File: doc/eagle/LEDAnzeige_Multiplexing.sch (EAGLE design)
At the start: 13 parts, among them IC4 MAX7219CNG

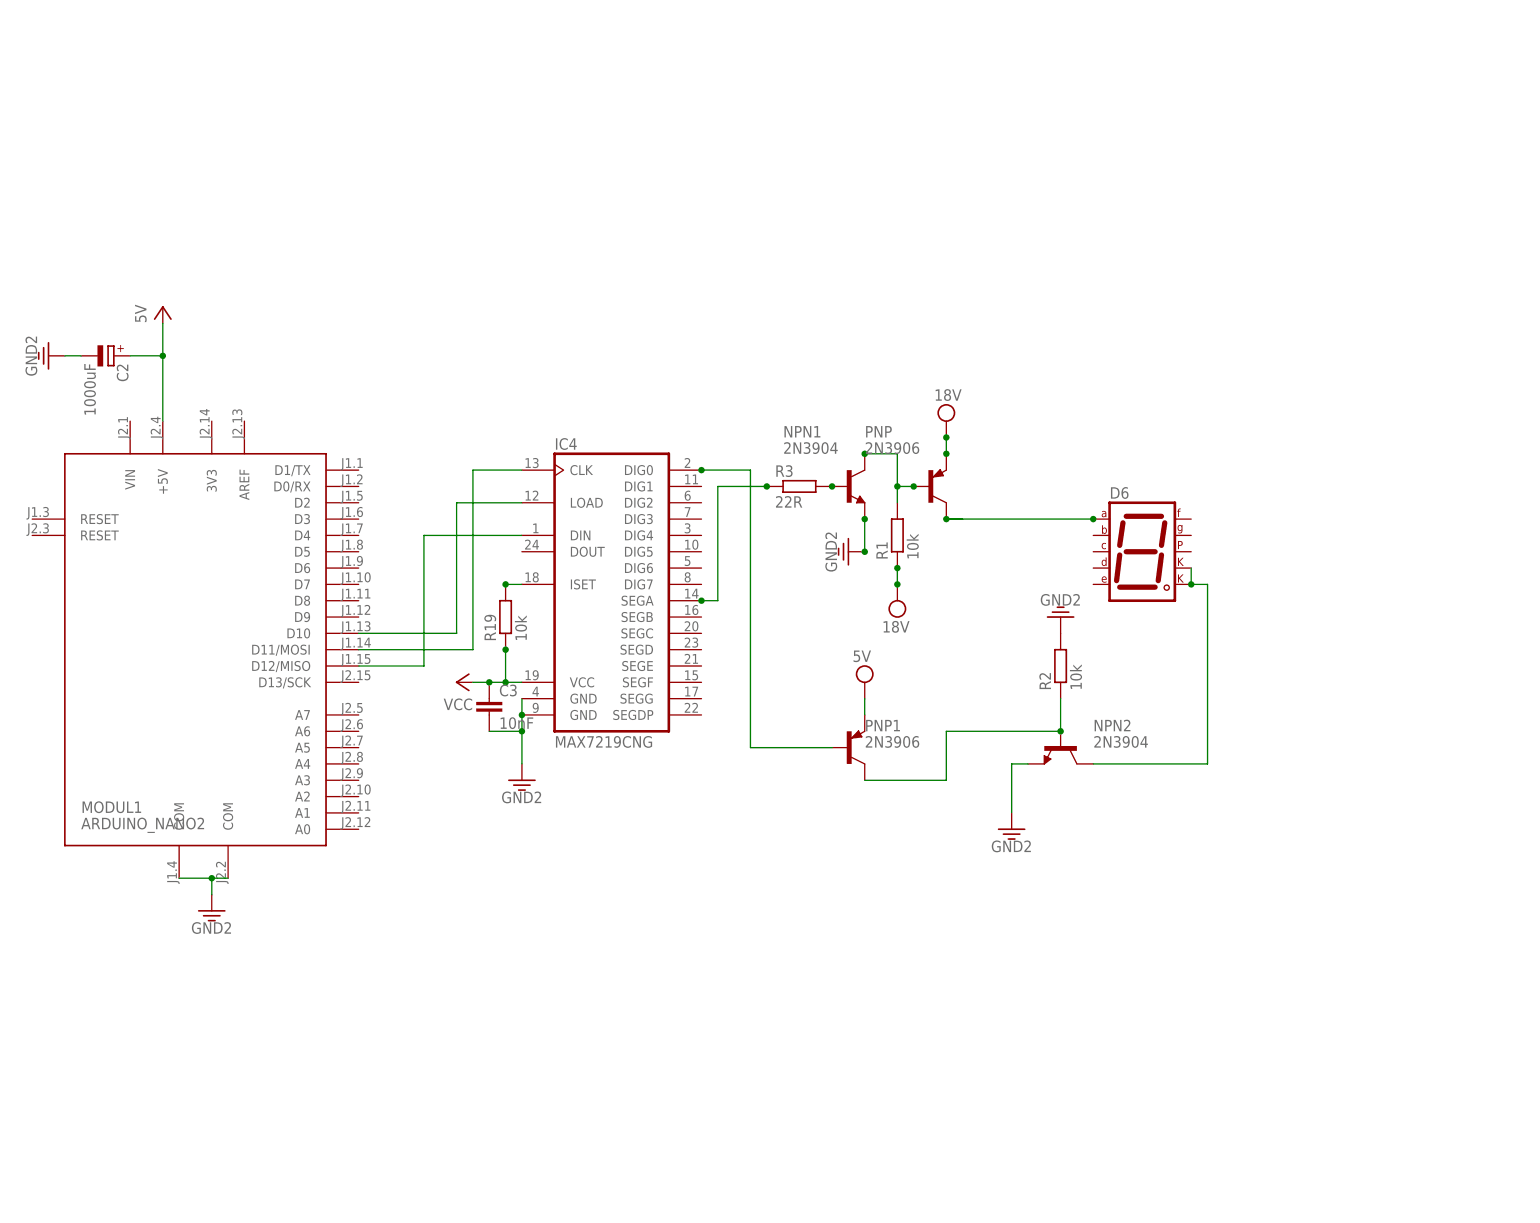
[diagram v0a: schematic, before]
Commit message: Schematic updated + Refactoring
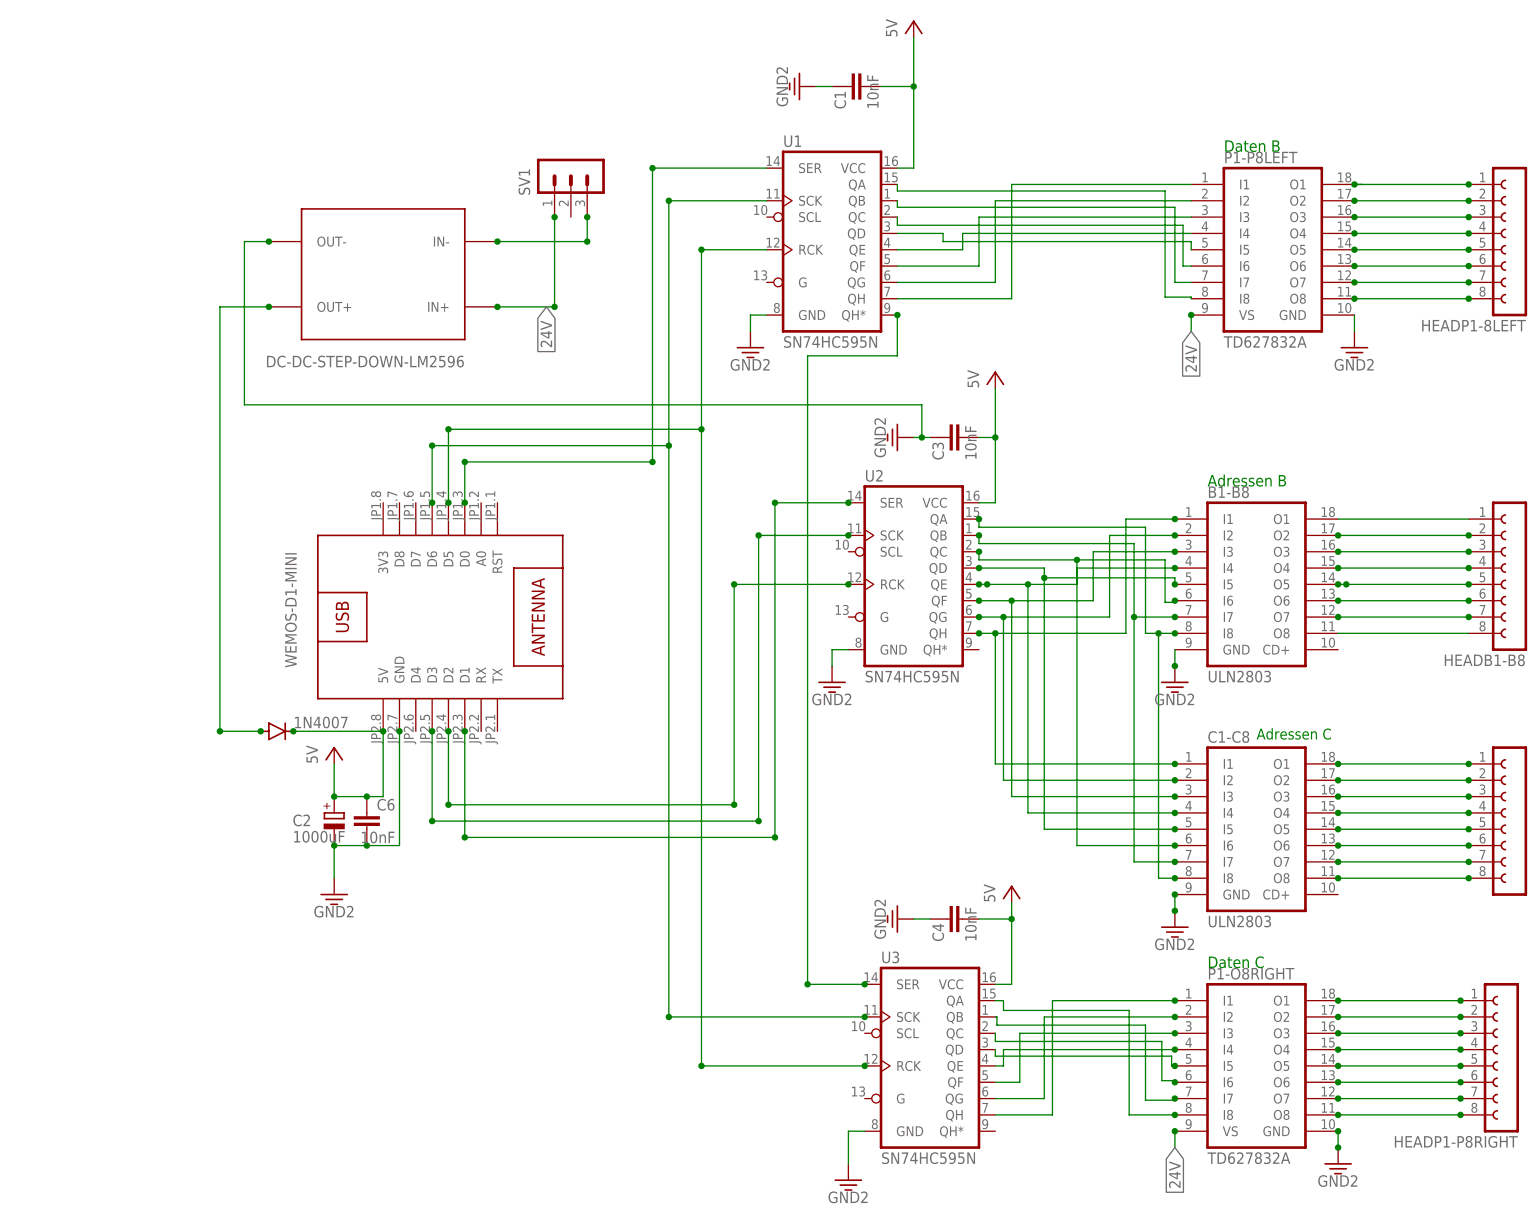
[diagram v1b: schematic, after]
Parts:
- removed D6: (no value), special:7SEG-MCK
- removed IC4: MAX7219CNG, maxim:MAX7219CNG
- removed MODUL1: ARDUINO_NANO2, arduino:ARDUINO_NANO2
- removed NPN1, NPN2: 2N3904, transistor-npn:2N3904
- removed PNP, PNP1: 2N3906, transistor-pnp:2N3906
- removed R1, R19, R2: 10k, resistor:R-EU_0204/7
- removed R3: 22R, resistor:R-EU_0204/7
- added 1N4007: (no value), diode:DIODE-D-2.5
- added B1-B8, C1-C8: ULN2803, uln-udn:ULN2803A
- added C1, C4, C6: 10nF, resistor:C-EU025-025X050
- added HEADB1-B8, HEADC1-C8, HEADP1-8LEFT, HEADP1-P8RIGHT: (no value), con-lsta:FE08-1
- added P1-O8RIGHT, P1-P8LEFT: TD627832A, td62083-dil:TD627832A
- added SV1: (no value), con-lstb:MA03-1
- added U$1: WEMOS-D1-MINI, diy-modules:WEMOS-D1-MINI
- added U$2: DC-DC-STEP-DOWN-LM2596, diy-modules_lm2596:DC-DC-STEP-DOWN-LM2596
- added U1, U2, U3: SN74HC595N, SparkFun-IC-Logic:74HC595N
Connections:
- removed net 3.3V: C2.-, C3.2, IC4.GND@1, IC4.GND@2, MODUL1.COM, MODUL1.COM@1, NPN1.E, NPN2.E, R2.2
- removed net N$101: IC4.CLK, MODUL1.D11/MOSI
- removed net N$102: IC4.LOAD, MODUL1.D10
- removed net N$103: IC4.DIN, MODUL1.D12/MISO
- new net 24V: P1-O8RIGHT.VS, P1-P8LEFT.VS, SV1.1, U$2.IN+
- new net GND: B1-B8.GND, C1-C8.GND, C1.1, C2.-, C3.1, C4.1, C6.2, P1-O8RIGHT.GND, P1-P8LEFT.GND, U$1.GND, U$2.OUT-, U1.GND, U2.GND, U3.GND
- new net N$10: HEADP1-8LEFT.3, P1-P8LEFT.O3
- new net N$11: HEADP1-8LEFT.4, P1-P8LEFT.O4
- new net N$12: HEADP1-8LEFT.5, P1-P8LEFT.O5
- new net N$13: HEADP1-8LEFT.6, P1-P8LEFT.O6
- new net N$14: HEADP1-8LEFT.7, P1-P8LEFT.O7
- new net N$15: HEADP1-8LEFT.8, P1-P8LEFT.O8
- new net N$16: B1-B8.O1, HEADB1-B8.1
- new net N$17: B1-B8.O2, HEADB1-B8.2
- new net N$18: B1-B8.O3, HEADB1-B8.3
- new net N$19: B1-B8.O4, HEADB1-B8.4
- new net N$20: HEADP1-8LEFT.1, P1-P8LEFT.O1
- new net N$21: B1-B8.O5, HEADB1-B8.5
- new net N$23: B1-B8.O7, HEADB1-B8.7
- new net N$24: B1-B8.O8, HEADB1-B8.8
- new net N$25: P1-P8LEFT.I1, U1.QH
- new net N$26: HEADP1-P8RIGHT.1, P1-O8RIGHT.O1
- new net N$27: P1-P8LEFT.I2, U1.QG
- new net N$28: HEADP1-P8RIGHT.3, P1-O8RIGHT.O3
- new net N$29: P1-P8LEFT.I3, U1.QF
- new net N$30: HEADP1-P8RIGHT.2, P1-O8RIGHT.O2
- new net N$31: P1-P8LEFT.I4, U1.QE
- new net N$32: P1-P8LEFT.I5, U1.QD
- new net N$33: HEADP1-P8RIGHT.5, P1-O8RIGHT.O5
- new net N$34: U$1.D0, U1.SER
- new net N$35: HEADP1-P8RIGHT.6, P1-O8RIGHT.O6
- new net N$37: U$1.D1, U2.SER
- new net N$39: HEADP1-P8RIGHT.4, P1-O8RIGHT.O4
- new net N$40: HEADP1-P8RIGHT.7, P1-O8RIGHT.O7
- new net N$42: P1-P8LEFT.I7, U1.QB
- new net N$43: P1-P8LEFT.I8, U1.QA
- new net N$44: P1-O8RIGHT.I2, U3.QG
- new net N$45: P1-O8RIGHT.I3, U3.QF
- new net N$46: P1-O8RIGHT.I4, U3.QE
- new net N$47: P1-O8RIGHT.I5, U3.QD
- new net N$48: P1-O8RIGHT.I6, U3.QC
- new net N$49: HEADP1-P8RIGHT.8, P1-O8RIGHT.O8
- new net N$5: B1-B8.I5, C1-C8.I5, U2.QD
- new net N$51: C1-C8.O2, HEADC1-C8.2
- new net N$52: C1-C8.O3, HEADC1-C8.3
- new net N$53: C1-C8.O4, HEADC1-C8.4
- new net N$54: C1-C8.O5, HEADC1-C8.5
- new net N$55: P1-O8RIGHT.I7, U3.QB
- new net N$56: P1-O8RIGHT.I8, U3.QA
- new net N$57: C1-C8.O6, HEADC1-C8.6
- new net N$58: C1-C8.O7, HEADC1-C8.7
- new net N$59: C1-C8.O8, HEADC1-C8.8
- new net N$60: U$1.D2, U2.RCK
- new net N$61: SV1.3, U$2.IN-
- new net N$69: 1N4007.A, U$2.OUT+
- new net N$7: B1-B8.I1, C1-C8.I1, U2.QH
- new net N$72: P1-O8RIGHT.I1, U3.QH
- new net N$74: U$1.D5, U1.RCK, U3.RCK
- new net N$76: U$1.D6, U1.SCK, U3.SCK
- new net N$8: B1-B8.I8, C1-C8.I8, U2.QA
- new net N$80: U$1.D3, U2.SCK
- new net N$9: HEADP1-8LEFT.2, P1-P8LEFT.O2
- new net N$92: U1.QH*, U3.SER
- net N$1: now also B1-B8.I7, C1-C8.I7, U2.QB; no longer D6.CK1, D6.CK2, NPN2.C
- net N$2: now also B1-B8.I2, C1-C8.I2, U2.QG; no longer IC4.DIG0, PNP1.B
- net N$22: now also B1-B8.O6, HEADB1-B8.6; no longer D6.A, PNP.C
- net N$3: now also B1-B8.I3, C1-C8.I3, U2.QF; no longer NPN1.B, R3.2
- net N$4: now also B1-B8.I4, C1-C8.I4, U2.QE; no longer NPN1.C, PNP.B, R1.2
- net N$41: now also P1-P8LEFT.I6, U1.QC; no longer IC4.SEGA, R3.1
- net N$50: now also C1-C8.O1, HEADC1-C8.1; no longer IC4.ISET, R19.2
- net N$6: now also B1-B8.I6, C1-C8.I6, U2.QC; no longer NPN2.B, PNP1.C, R2.1
- net VCC: now also 1N4007.C, C1.2, C3.2, C4.2, C6.1, U$1.5V, U1.VCC, U2.VCC, U3.VCC; no longer C3.1, IC4.VCC, MODUL1.+5V, PNP.E, PNP1.E, R1.1, R19.1
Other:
- note added: "Adressen B"
- note added: "Adressen C"
- note added: "Daten B"
- note added: "Daten C"
- moved on the sheet: C2, C3

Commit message: Board updated
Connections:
- net GND: now also U1.G, U2.G, U3.G
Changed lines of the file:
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@@
 <pinref part="U1" gate="U1" pin="GND"/>
 <wire x1="-114.3" y1="59.69" x2="-111.76" y2="59.69" width="0.1524" layer="91"/>
+<pinref part="U1" gate="U1" pin="G"/>
+<wire x1="-111.76" y1="64.77" x2="-114.3" y2="64.77" width="0.1524" layer="91"/>
+<wire x1="-114.3" y1="64.77" x2="-114.3" y2="59.69" width="0.1524" layer="91"/>
+<junction x="-114.3" y="59.69"/>
+<junction x="-111.76" y="64.77"/>
+<junction x="-114.3" y="64.77"/>
+<junction x="-111.76" y="59.69"/>
 </segment>
 <segment>
@@
 <wire x1="-101.6" y1="7.62" x2="-101.6" y2="5.08" width="0.1524" layer="91"/>
 <pinref part="GND1" gate="G$1" pin="3.3V"/>
+<pinref part="U2" gate="U1" pin="G"/>
+<wire x1="-99.06" y1="12.7" x2="-101.6" y2="12.7" width="0.1524" layer="91"/>
+<wire x1="-101.6" y1="12.7" x2="-101.6" y2="7.62" width="0.1524" layer="91"/>
+<junction x="-101.6" y="7.62"/>
+<junction x="-99.06" y="12.7"/>
+<junction x="-101.6" y="12.7"/>
 </segment>
 <segment>
@@
 <segment>
 <pinref part="GND8" gate="G$1" pin="3.3V"/>
-<wire x1="-99.06" y1="-72.39" x2="-99.06" y2="-67.31" width="0.1524" layer="91"/>
+<wire x1="-99.06" y1="-72.39" x2="-99.06" y2="-68.58" width="0.1524" layer="91"/>
 <pinref part="U3" gate="U1" pin="GND"/>
+<wire x1="-99.06" y1="-68.58" x2="-99.06" y2="-67.31" width="0.1524" layer="91"/>
 <wire x1="-99.06" y1="-67.31" x2="-96.52" y2="-67.31" width="0.1524" layer="91"/>
+<pinref part="U3" gate="U1" pin="G"/>
+<wire x1="-96.52" y1="-62.23" x2="-99.06" y2="-62.23" width="0.1524" layer="91"/>
+<wire x1="-99.06" y1="-62.23" x2="-99.06" y2="-67.31" width="0.1524" layer="91"/>
+<junction x="-99.06" y="-67.31"/>
+<junction x="-99.06" y="-62.23"/>
+<junction x="-96.52" y="-62.23"/>
+<junction x="-96.52" y="-67.31"/>
 </segment>
 <segment>
